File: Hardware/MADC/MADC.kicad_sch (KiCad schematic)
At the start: 34 parts, among them J1 Conn_02x04_Counter_Clockwise, J3 Conn_02x03_Counter_Clockwise, U1 LM311PWR, U2 OPA192IDBVT, U3 OPA140AIDBVT, U4 OPA2192IDGKT, U5 DG419LEUA, U6 DG211BDQ-T1-E3

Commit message: PCB
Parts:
- removed C8: 0.1u, Capacitor_SMD:C_0402_1005Metric_Pad0.74x0.62mm_HandSolder, symbol Device:C
- added C1, C10, C11, C2, C3, C4, C5: 0.1u, Capacitor_SMD:C_0402_1005Metric_Pad0.74x0.62mm_HandSolder, symbol Device:C
- D1, D2: value BAV21W-E3-08 -> 1N4448WT; footprint Diode_SMD:D_SOD-123 -> Diode_SMD:D_SOD-323; symbol Device:D -> Diode:1N4448WS
- J2: renamed from J3; footprint Connector_PinHeader_1.27mm:PinHeader_2x03_P1.27mm_Vertical_SMD -> Connector_PinHeader_1.27mm:PinHeader_2x04_P1.27mm_Vertical_SMD; symbol Connector_Generic:Conn_02x03_Counter_Clockwise -> Connector_Generic:Conn_02x04_Counter_Clockwise
- renumbered C2 to C12, C3 to C13, C4 to C14, C1 to C15, C5 to C6, C6 to C7, C7 to C8, R11 to R1, R6 to R10, R5 to R11, R4 to R12, R12 to R2, R10 to R3, R9 to R4, R7 to R5, R8 to R6, R2 to R7, R1 to R8, R3 to R9, RN3 to RN2, RN2 to RN3, U6 to U1, U5 to U2, U4 to U3, U3 to U4, U2 to U5, U1 to U6
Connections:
- net +3.3V: now also J1.2 (Pin_2), C1.2, C2.2; no longer J1.8 (Pin_8)
- net -7V: now also J2.8 (Pin_8); no longer J2.6 (Pin_6)
- net AD_CMP: now also J1.3 (Pin_3); no longer J1.7 (Pin_7)
- net AD_ID: now also J1.8 (Pin_8); no longer J1.3 (Pin_3)
- net AD_IIN: now also J1.6 (Pin_6); no longer J1.4 (Pin_4)
- net AD_IN: now also J2.3 (Pin_3), J2.5 (Pin_5); no longer J2.2 (Pin_2)
- net AD_IRN: now also J1.4 (Pin_4); no longer J1.2 (Pin_2)
- net AD_IRP: now also J1.7 (Pin_7); no longer J1.6 (Pin_6)
- net GNDA: now also J2.2 (Pin_2), J2.4 (Pin_4), C10.1, C11.1, C3.1, C4.1, C5.1; no longer J2.3 (Pin_3)
- net GNDD: now also C1.1, C2.1
- net VCC: now also J2.6 (Pin_6), C3.2, C4.2, C5.2; no longer J2.4 (Pin_4)
- net VEE: now also J2.7 (Pin_7), C10.2, C11.2; no longer J2.5 (Pin_5)
- net at U3.3 (+): now also U2.1

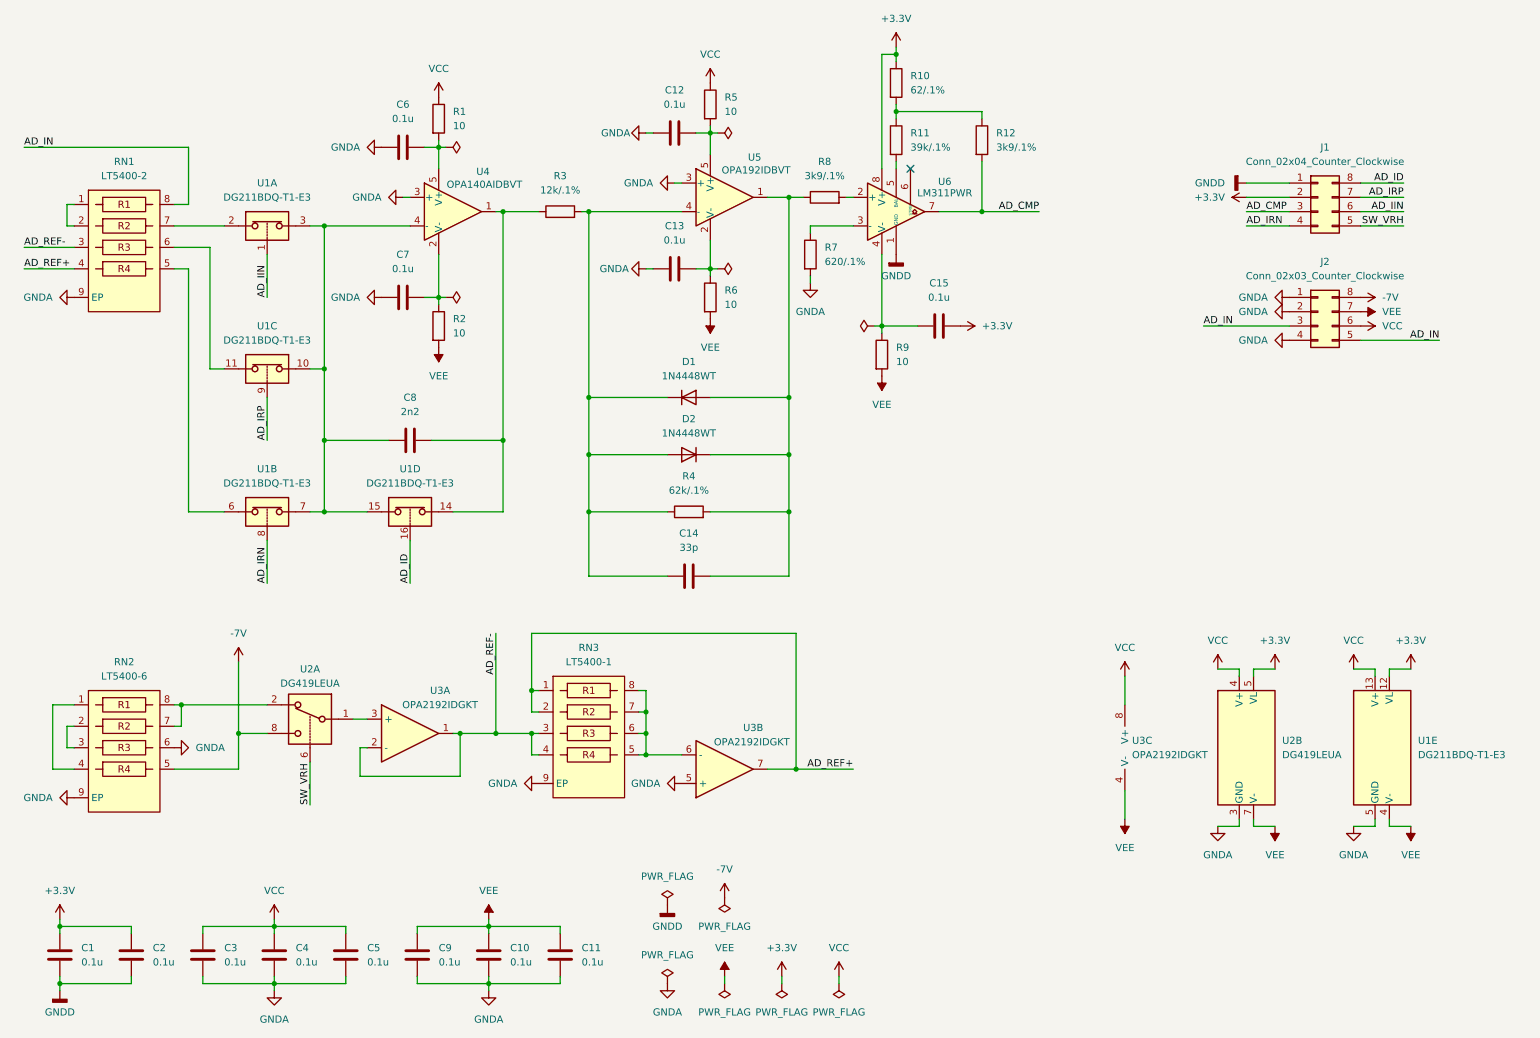
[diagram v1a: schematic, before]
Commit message: MADC module send to production
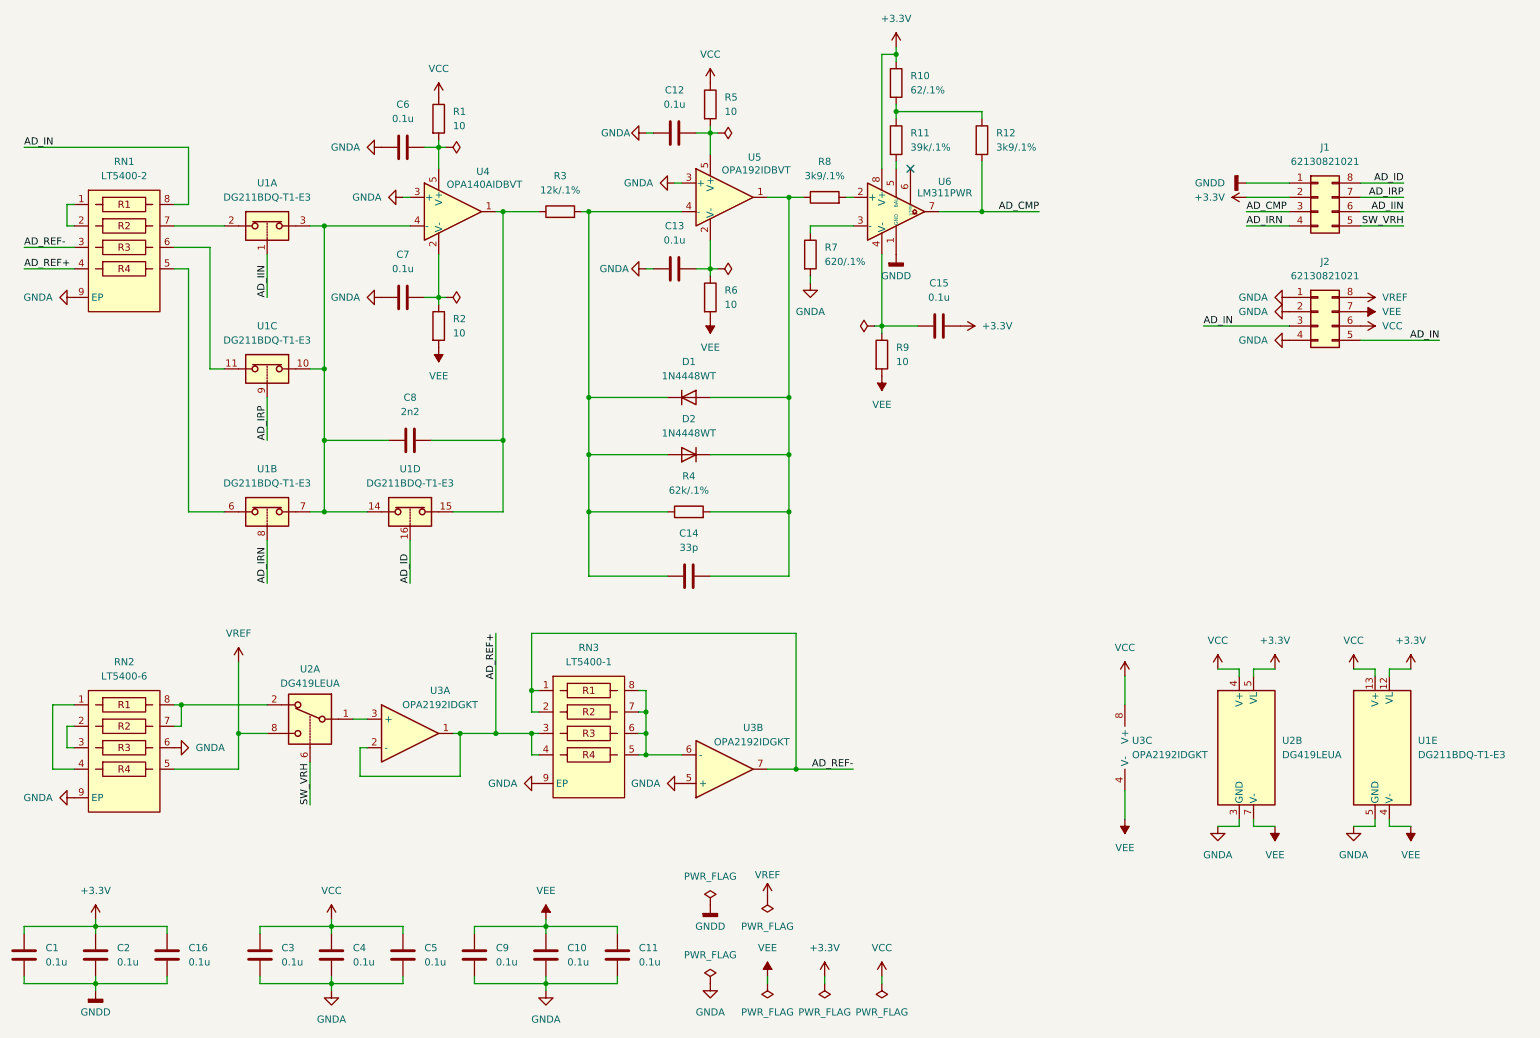
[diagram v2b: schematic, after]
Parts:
- added C16: 0.1u, Capacitor_SMD:C_0402_1005Metric_Pad0.74x0.62mm_HandSolder, symbol Device:C
- J1: value Conn_02x04_Counter_Clockwise -> 62130821021
- J2: value Conn_02x03_Counter_Clockwise -> 62130821021
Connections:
- net +3.3V: now also C16.2
- net AD_REF+: now also RN3.3, RN3.4, U3.1, U3.2 (-); no longer RN3.1, RN3.2, U3.7
- net AD_REF-: now also RN3.1, RN3.2, U3.7; no longer RN3.3, RN3.4, U3.1, U3.2 (-)
- net GNDD: now also C16.1
- net at C8.1, U1.10, U1.3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: now also U1.14; no longer U1.15
- net at C8.2, R3.1, U4.1: now also U1.15; no longer U1.14
- net -7V renamed VREF
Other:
- moved on the sheet: C1, C10, C11, C2, C3, C4, C5, C9
